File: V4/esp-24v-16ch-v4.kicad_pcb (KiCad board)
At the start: 4 copper layers, 108 x 67.8 mm, 302 parts, among them J1 DB141V-2.54-8P, J2 DB141V-2.54-8P, J3 DB141V-2.54-8P, J4 DB141V-2.54-8P, J5 VIN, J6 USB_C_Receptacle_USB2.0, J7 ETHERNET, J8 NTC, Q1 WPM2015-3/TR, Q10 MMBT2222A, Q11 MMBT2222A, Q12 MMBT2222A, Q13 MMBT2222A, Q14 MMBT2222A, Q15 MMBT2222A, Q16 MMBT2222A, Q17 MMBT2222A, Q18 MMBT2222A, Q19 MMBT2222A, Q2 MMUN2211LT3G, Q3 UMH3N, Q4 MMBT2222A, Q5 MMBT2222A, Q6 MMBT2222A, Q7 MMBT2222A, Q8 MMBT2222A, Q9 MMBT2222A, SW1 RESET, U1 SY8089A1AAC, U10 OR-3H7-4, U11 OR-3H7-4, U12 OR-3H7-4, U13 OR-3H7-4, U2 TX4138, U3 CH340C, U4 ESP32-WROOM-32UE-N16, U5 LAN8710A, U6 MCP23017_SS, U7 ADS1115IDGS, U8 MCP23017_SS, U9 AHT20

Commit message: Replaced temp/humid sensor for SHT31
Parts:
- U9: value AHT20 -> SHT31-DIS; footprint Tales:DFN-6-3x3mm_P1mm -> Tales:Sensirion_DFN-8-1EP_2.5x2.5mm_P0.5mm_EP1.1x1.7mm
- moved U9 0.37 mm to (148.8, 103.1), turned to 0 degrees
- moved C26 0.30 mm to (154.8, 103.1)
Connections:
- U9 pad 1: unconnected-(U9-NC-Pad1) -> /MCU/I2C_SDA
- U9 pad 2: +3.3V -> GND
- U9 pad 3: /MCU/I2C_SCL -> unconnected-(U9-ALERT-Pad3)
- U9 pad 4: /MCU/I2C_SDA -> /MCU/I2C_SCL
- U9 pad 5: GND -> +3.3V
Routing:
- net /MCU/I2C_SCL: track 115.2 -> 119.2 mm
- net +3.3V: track 263.9 -> 260.6 mm
- net /MCU/I2C_SDA: track 116.6 -> 119.6 mm
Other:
- outline, holes or cut-outs redrawn

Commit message: Final tweaks. For now.
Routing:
- net /MCU/I2C_SDA: track 119.6 -> 121.1 mm
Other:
- outline, holes or cut-outs redrawn

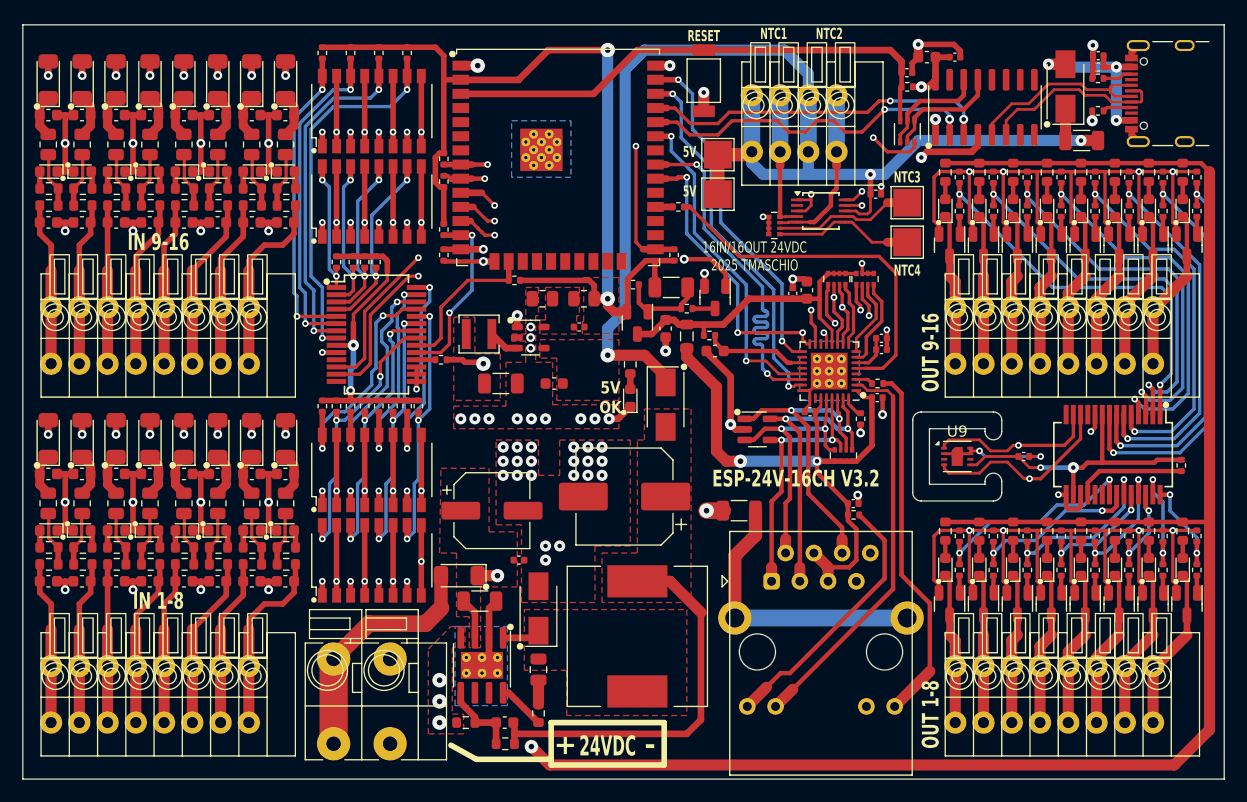
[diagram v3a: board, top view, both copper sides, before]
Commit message: Updated to 2 NTCs instead of 4.
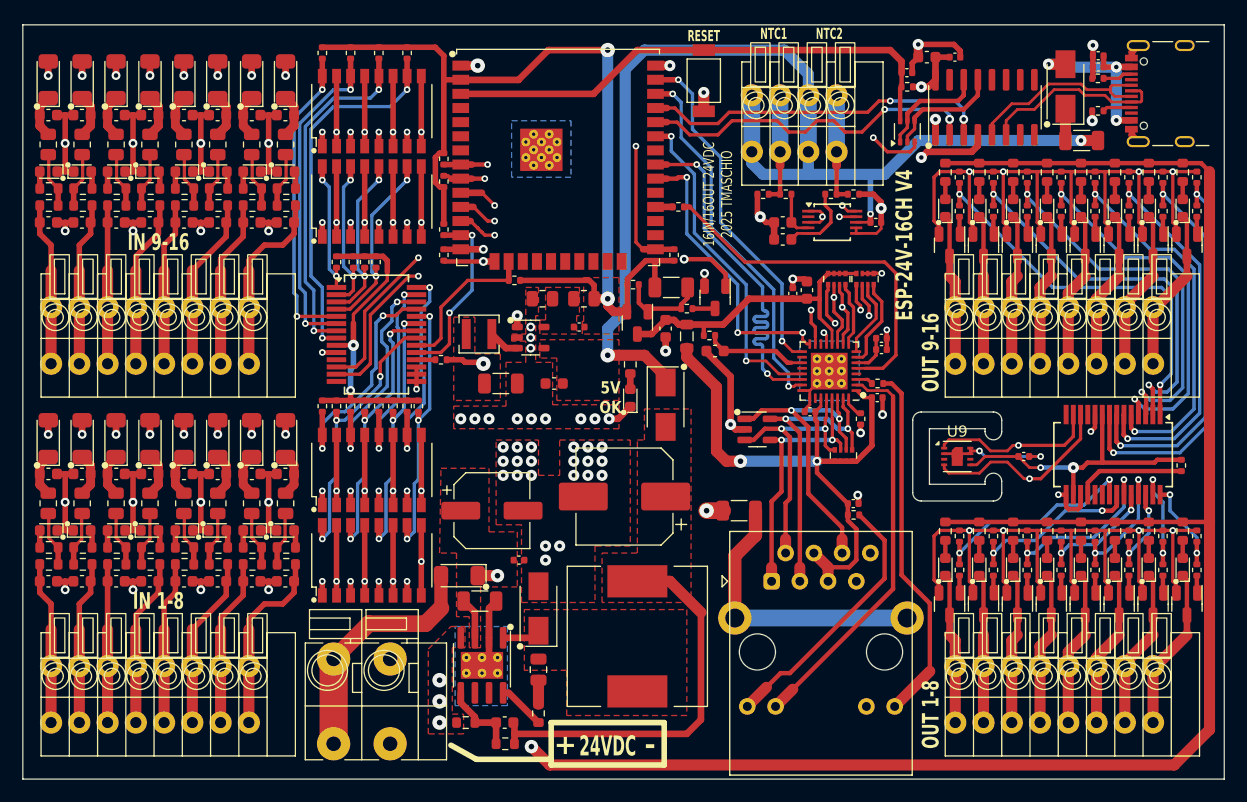
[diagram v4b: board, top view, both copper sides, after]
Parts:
- removed H1, H2: +5V, TestPoint:TestPoint_Pad_2.5x2.5mm
- removed H3: AIN2, TestPoint:TestPoint_Pad_2.5x2.5mm
- removed H4: AIN3, TestPoint:TestPoint_Pad_2.5x2.5mm
- removed RN4: 4x3k/62,5mW, Tales:R_Array_Convex_4x0402
- added C59: 33nF/50V, Tales:C_0603_1608Metric, F.Cu at (133.1, 82.0)
- added C60: 33nF/50V, Tales:C_0603_1608Metric, F.Cu at (133.1, 83.6)
- added R122: 10k/62,5mW, Tales:R_0402_1005Metric, F.Cu at (131.3, 79.5)
- added R123: 10k/62,5mW, Tales:R_0402_1005Metric, F.Cu at (139.4, 79.5)
- added R124: 1k/62,5mW, Tales:R_0402_1005Metric, F.Cu at (133.4, 79.5)
- added R125: 1k/62,5mW, Tales:R_0402_1005Metric, F.Cu at (137.4, 79.5)
- Q3: footprint Tales:SOT-363_SC-70-6 -> Package_TO_SOT_SMD:SOT-363_SC-70-6
- U6, U8: footprint Tales:SSOP-28_5.3x10.2mm_P0.65mm -> Package_SO:SSOP-28_5.3x10.2mm_P0.65mm
- moved C25 2.54 mm to (141.4, 82.0)
- moved U7 1.44 mm to (137.5, 82.0)
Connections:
- U7 pad 4: Net-(J8-Pin_2) -> Net-(U7-AIN0)
- U7 pad 5: Net-(J8-Pin_4) -> Net-(U7-AIN1)
- U7 pad 6: Net-(RN4-R4.2) -> GND
- U7 pad 7: Net-(RN4-R3.2) -> GND
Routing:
- net Net-(RN4-R4.2): track 12.6 -> 0.00 mm
- net Net-(RN4-R3.2): track 12.6 -> 0.00 mm
- net GND: track 400.4 -> 409.7 mm
- net Net-(U7-AIN1): track 0.00 -> 6.94 mm
- net +5V: track 122.8 -> 115.9 mm
- net Net-(J8-Pin_4): track 15.3 -> 9.91 mm
- net Net-(U7-AIN0): track 0.00 -> 4.27 mm
- net Net-(J8-Pin_2): track 12.5 -> 9.91 mm
- net /MCU/I2C_SCL: track 119.6 -> 117.4 mm
- net /MCU/I2C_SDA: track 121.1 -> 119.3 mm
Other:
- board text added: "ESP-24V-16CH V4"
- board text removed: "5V"
- board text removed: "ESP-24V-16CH V3.2"
- board text removed: "NTC3"
- board text removed: "NTC4"
